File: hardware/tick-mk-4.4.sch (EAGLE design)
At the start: 30 parts, among them IC1 ATMEGA328P, IC2 DS1338, IC3 L7805, Y1 16MHz

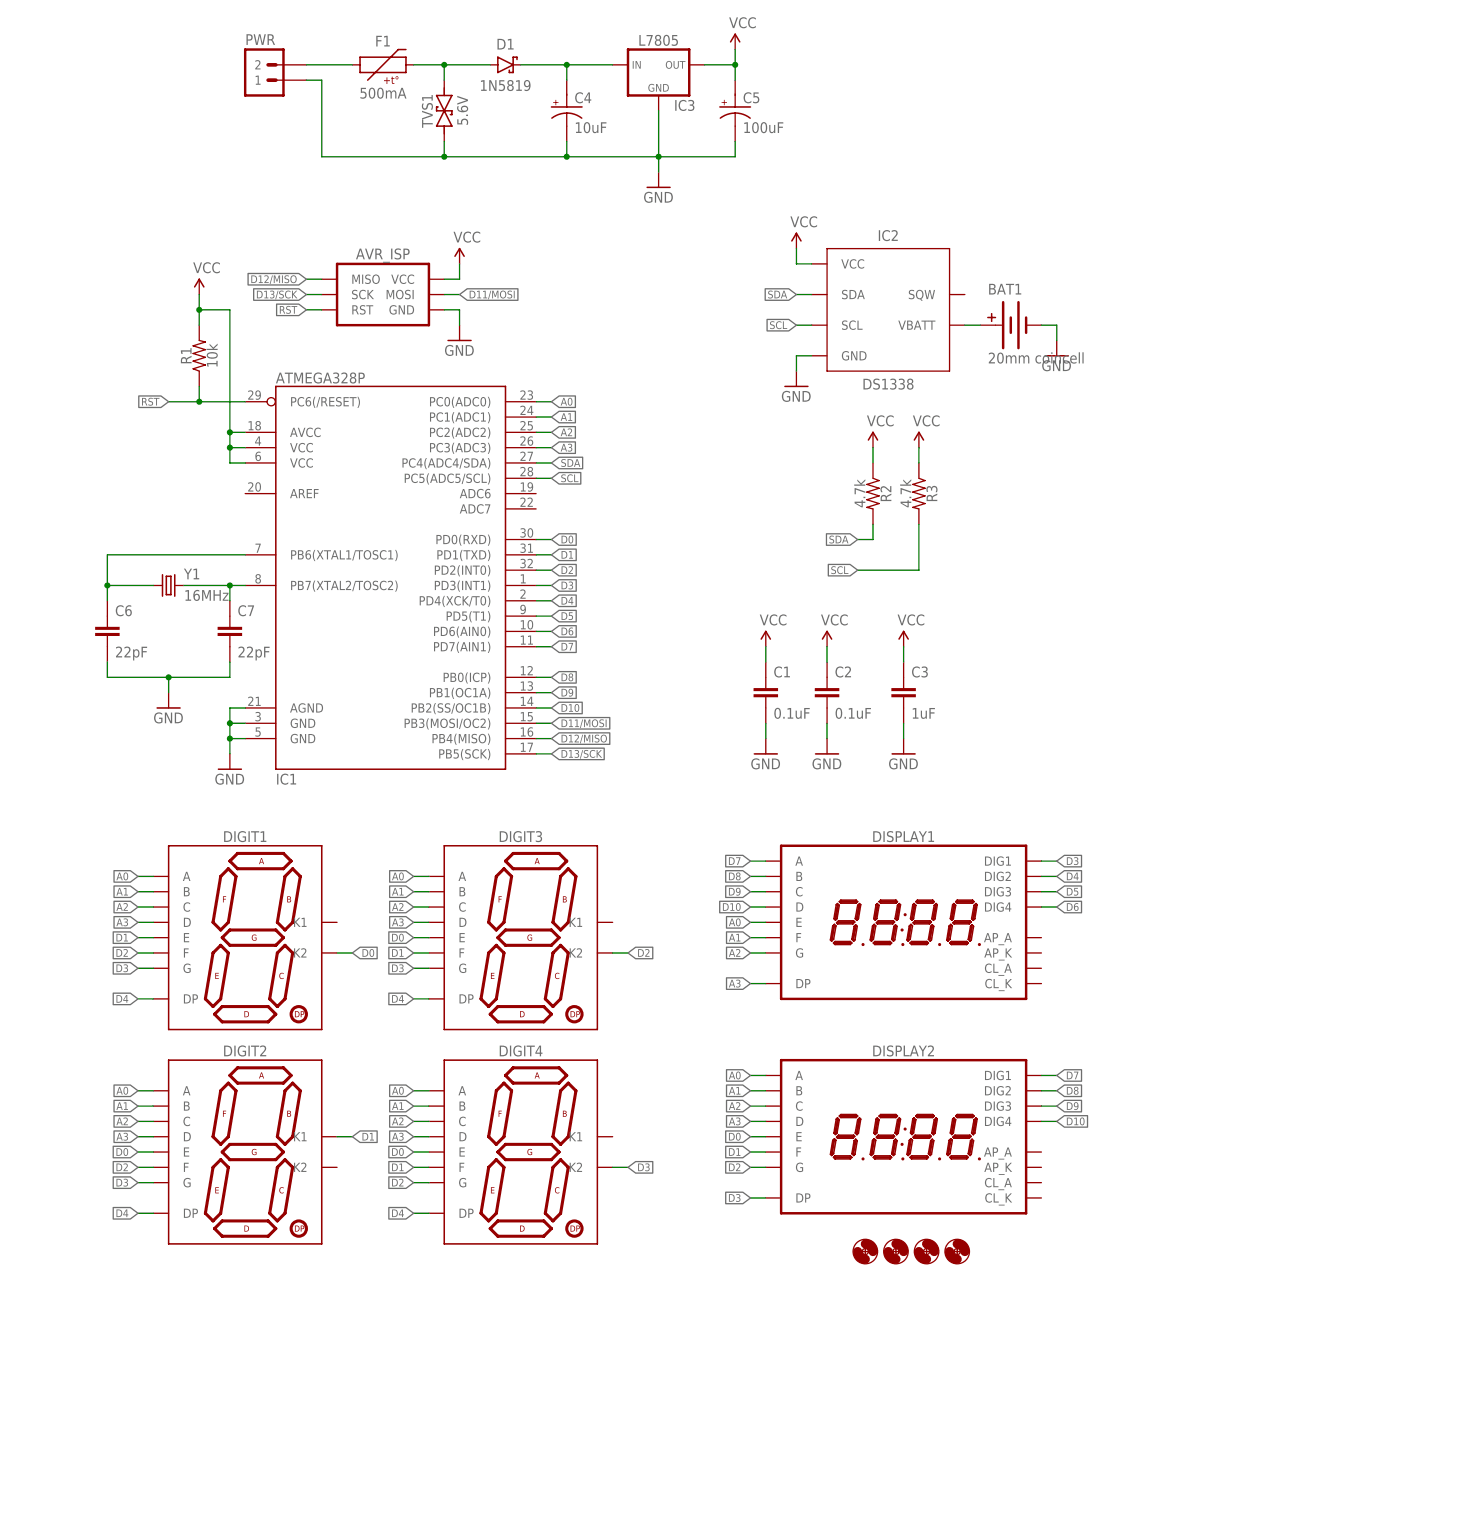
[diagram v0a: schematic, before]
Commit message: pth version done, way easier than expected
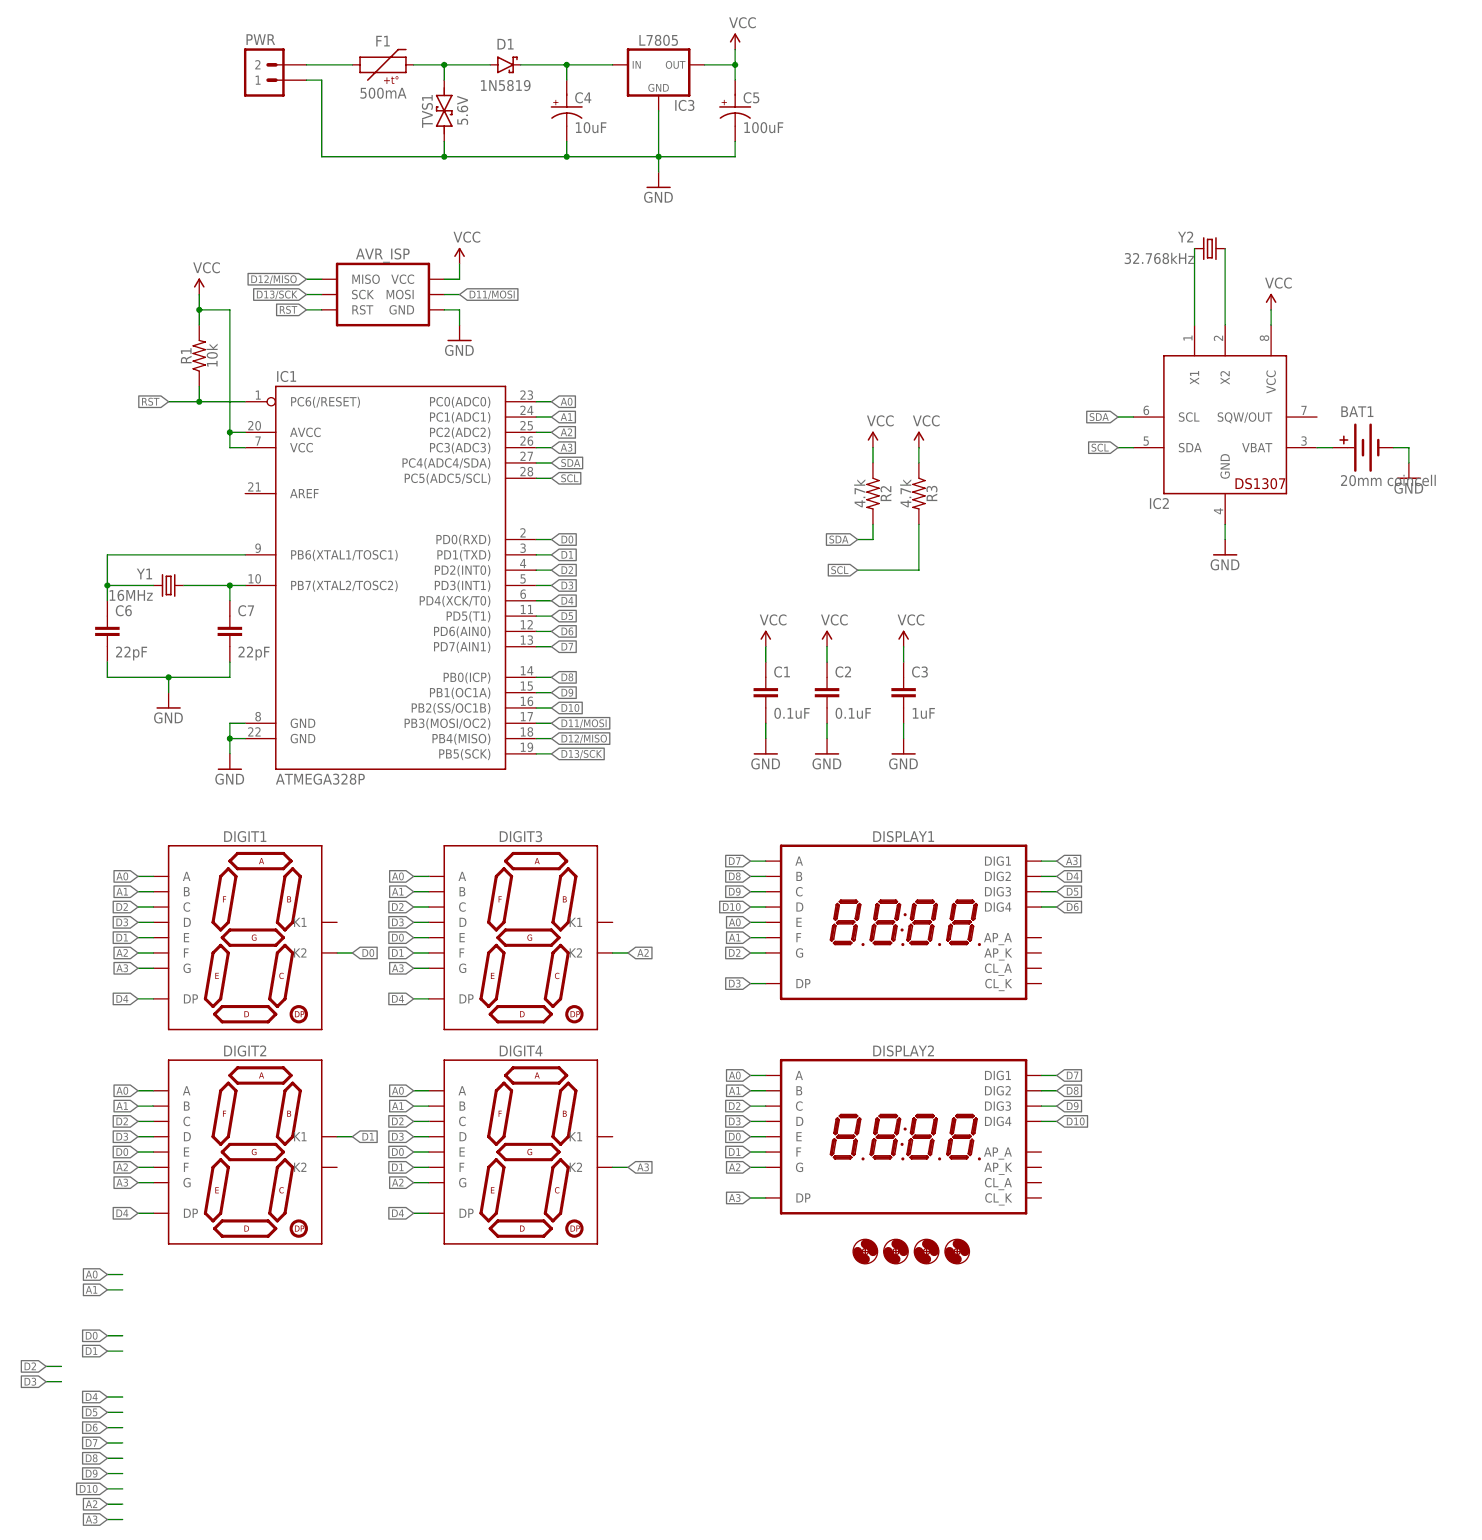
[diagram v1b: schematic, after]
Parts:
- added Y2: 32.768kHz, A_butts:CRYSTALTC26H
- IC1: device A_butts:ATMEGA328_SMT -> A_butts:ATMEGA328P_PDIP
- IC2: value DS1338 -> DS1307; device A_butts:DS1338CSOIC16W -> A_butts:DS1307
- R1, R2, R3: device A_butts:RESISTORPTH-AXIAL-6.35MM -> A_butts:RESISTORPTH-AXIAL-7.62MM
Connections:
- new net N$2: IC2.X1, Y2.2
- new net N$3: IC2.X2, Y2.1
- net A2: now also DIGIT1.F, DIGIT2.F, DIGIT3.K2, DIGIT4.G, DISPLAY2.G; no longer DIGIT1.C, DIGIT2.C, DIGIT3.C, DIGIT4.C, DISPLAY1.G, DISPLAY2.C
- net A3: now also DIGIT1.G, DIGIT2.G, DIGIT3.G, DIGIT4.K2, DISPLAY1.DIG1, DISPLAY2.DP; no longer DIGIT1.D, DIGIT2.D, DIGIT3.D, DIGIT4.D, DISPLAY1.DP, DISPLAY2.D
- net D2: now also DIGIT1.C, DIGIT2.C, DIGIT3.C, DIGIT4.C, DISPLAY1.G, DISPLAY2.C; no longer DIGIT1.F, DIGIT2.F, DIGIT3.K2, DIGIT4.G, DISPLAY2.G
- net D3: now also DIGIT1.D, DIGIT2.D, DIGIT3.D, DIGIT4.D, DISPLAY1.DP, DISPLAY2.D; no longer DIGIT1.G, DIGIT2.G, DIGIT3.G, DIGIT4.K2, DISPLAY1.DIG1, DISPLAY2.DP
- net GND: no longer IC1.AGND
- net N$1: now also IC2.VBAT; no longer IC2.VBATT
- net N$6: now also Y1.2; no longer Y1.1
- net N$9: now also Y1.1; no longer Y1.2
- net SCL: now also IC2.SDA; no longer IC2.SCL
- net SDA: now also IC2.SCL; no longer IC2.SDA
- net VCC: now also IC1.VCC; no longer IC1.VCC@1, IC1.VCC@2
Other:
- moved on the sheet: BAT1
